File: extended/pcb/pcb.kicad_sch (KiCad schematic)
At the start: 23 parts, among them J1 LED Out +24V, J2 LED Out data, J3 LED Out GND, J4 5V out, J5 Power in 24V, J6 MEZD71201A-G, J7 Power in GND, K1 AZ943-1CH-5DE, U1 WLED, U2 74HCT245

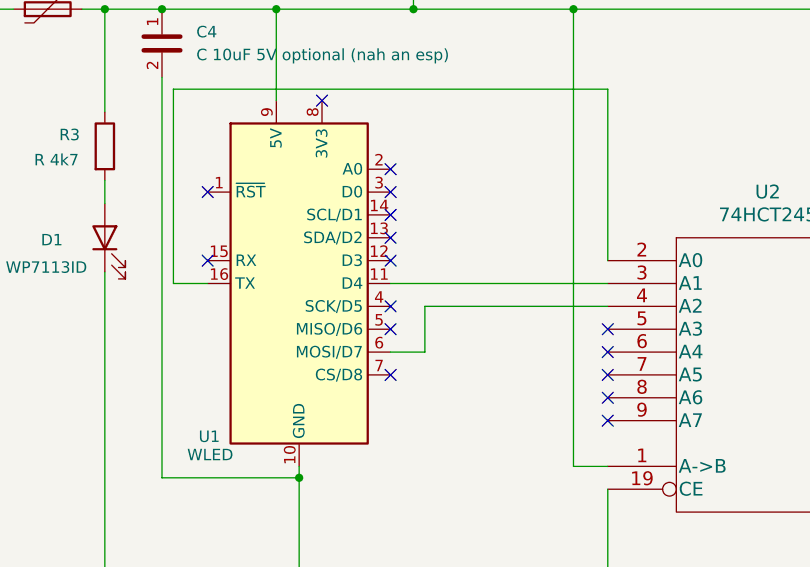
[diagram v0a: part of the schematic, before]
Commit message: fix relay flickering on boot
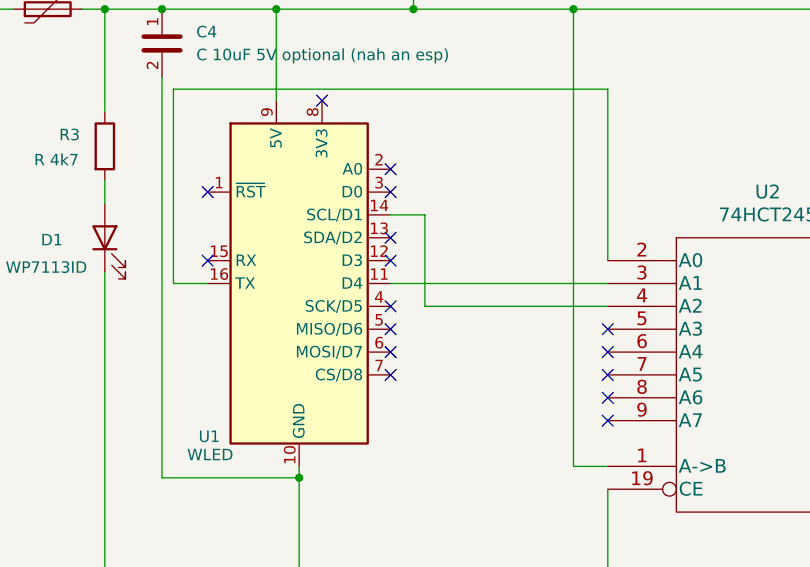
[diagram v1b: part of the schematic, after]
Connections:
- net at U2.4 (A2): now also U1.14 (SCL/D1); no longer U1.6 (MOSI/D7)
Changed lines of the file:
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@@
+	)
+	(no_connect
+		(at 116.84 93.98)
 	)
 	(no_connect
@@
 	)
 	(no_connect
-		(at 116.84 78.74)
-	)
-	(no_connect
 		(at 116.84 73.66)
 	)
@@
 	(wire
 		(pts
-			(xy 120.65 93.98) (xy 116.84 93.98)
-		)
-		(stroke
-			(width 0)
-			(type default)
-		)
-	)
-	(wire
-		(pts
 			(xy 85.09 55.88) (xy 85.09 67.31)
 		)
@@
 	(wire
 		(pts
+			(xy 116.84 78.74) (xy 120.65 78.74)
+		)
+		(stroke
+			(width 0)
+			(type default)
+		)
+	)
+	(wire
+		(pts
 			(xy 140.97 106.68) (xy 137.16 106.68)
 		)
@@
 	(wire
 		(pts
-			(xy 120.65 93.98) (xy 120.65 88.9)
-		)
-		(stroke
-			(width 0)
-			(type default)
-		)
-	)
-	(wire
-		(pts
 			(xy 106.68 106.68) (xy 106.68 107.95)
 		)
 		(stroke
+			(width 0)
+			(type default)
+		)
+	)
+	(wire
+		(pts
+			(xy 120.65 88.9) (xy 120.65 78.74)
+		)
+		(stroke

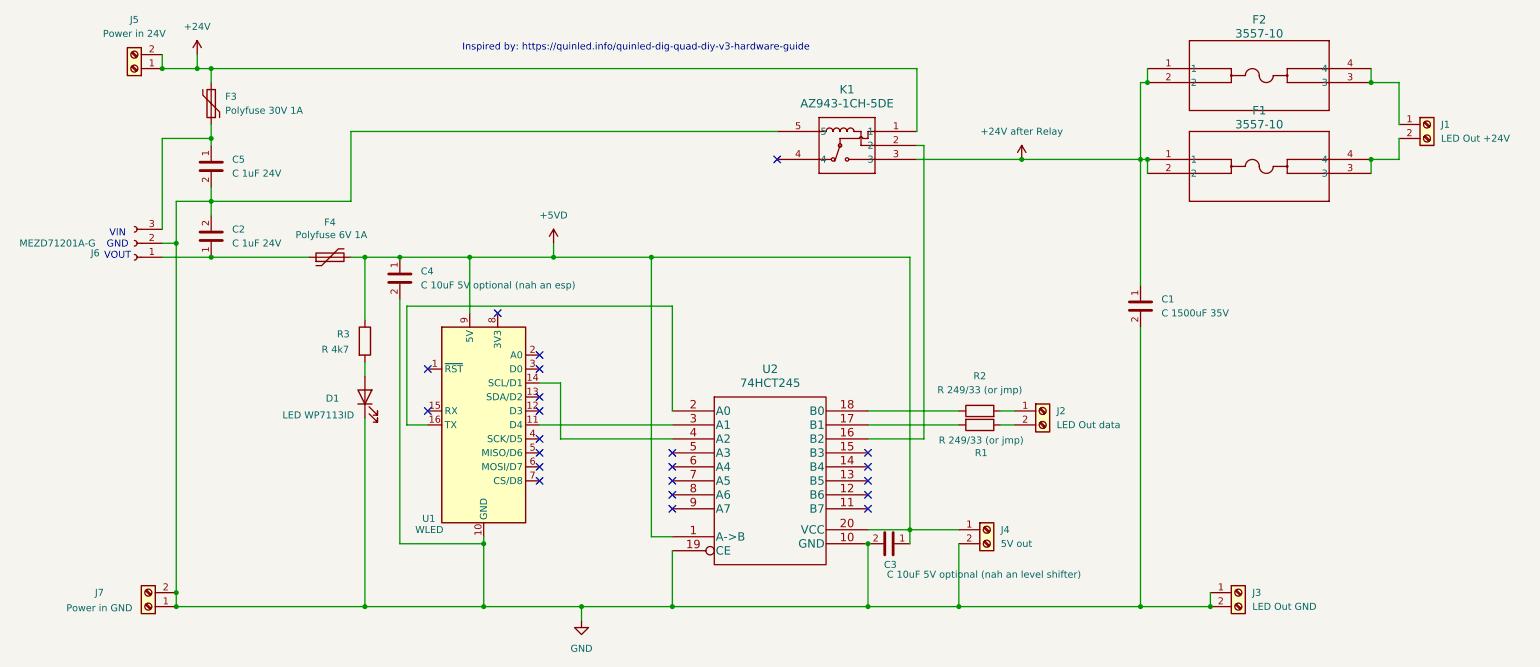
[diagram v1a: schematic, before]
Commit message: This commit is most probably wrong, but lets store it
The issue is that when the PCB is provided power then the led strip
quickly lights up, then goes of. Afterwards wled turns it on again.

I though this is because the wiring of the relay is wrong. The
documentation shows the default state to be in reverse of what the
downloadbale schematic provides
(https://www.azettler.com/pdfs/az943.pdf).
Then the relay would be on when no power is applied through the coil.

However that does not really match the sounds it makes. During the quick
on time of the led strip there are two click sounds instead of one which
should be the case if the above holds true.
Unless the relay per default clicks once when power is provided even
when the coil is low.
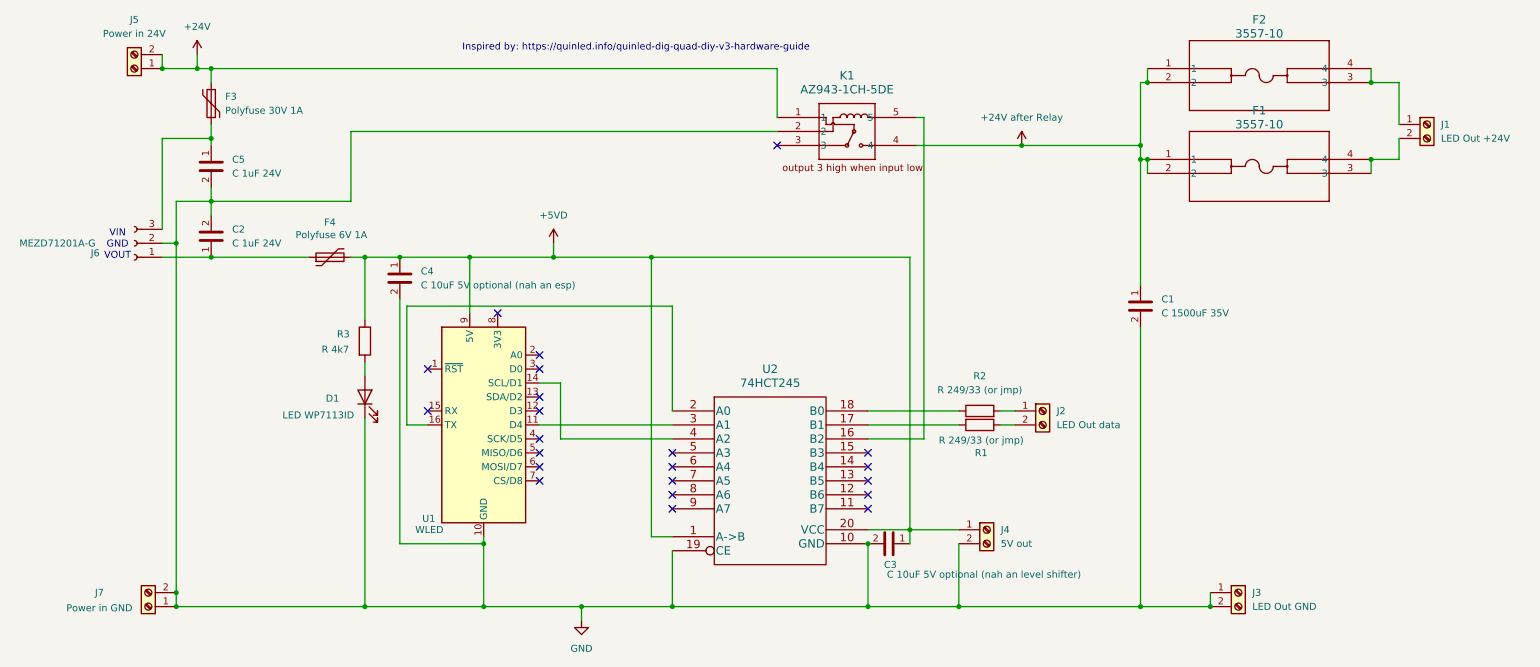
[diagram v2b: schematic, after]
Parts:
- K1: footprint Library:K_AZ943-1C_AMZ -> K_AZ943-1C_AMZ
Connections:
- net +24V after Relay: now also K1.4; no longer K1.3
- net GND: now also K1.2; no longer K1.5
- net at U2.16 (B2): now also K1.5; no longer K1.2
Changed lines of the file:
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@@
 	)
 	(junction
-		(at 204.47 38.1)
+		(at 57.15 21.59)
 		(diameter 0)
 		(color 0 0 0 0)
@@
 	)
 	(junction
+		(at 226.06 35.56)
+		(diameter 0)
+		(color 0 0 0 0)
+	)
+	(junction
 		(at 238.76 119.38)
 		(diameter 0)
@@
 	)
 	(junction
-		(at 57.15 21.59)
-		(diameter 0)
-		(color 0 0 0 0)
-	)
-	(junction
 		(at 119.38 55.88)
 		(diameter 0)
@@
 	(junction
 		(at 227.33 38.1)
+		(diameter 0)
+		(color 0 0 0 0)
+	)
+	(junction
+		(at 204.47 35.56)
 		(diameter 0)
 		(color 0 0 0 0)
@@
 	)
 	(no_connect
+		(at 160.02 35.56)
+	)
+	(no_connect
 		(at 140.97 91.44)
 	)
@@
 	)
 	(no_connect
-		(at 160.02 38.1)
-	)
-	(no_connect
 		(at 116.84 96.52)
 	)
@@
 	(wire
 		(pts
+			(xy 204.47 35.56) (xy 226.06 35.56)
+		)
+		(stroke
+			(width 0)
+			(type default)
+		)
+	)
+	(wire
+		(pts
 			(xy 57.15 55.88) (xy 74.93 55.88)
 		)
@@
 	(wire
 		(pts
-			(xy 185.42 38.1) (xy 204.47 38.1)
-		)
-		(stroke
-			(width 0)
-			(type default)
-		)
-	)
-	(wire
-		(pts
 			(xy 48.26 50.8) (xy 48.26 34.29)
 		)
@@
 	(wire
 		(pts
+			(xy 185.42 35.56) (xy 204.47 35.56)
+		)
+		(stroke
+			(width 0)
+			(type default)
+		)
+	)
+	(wire
+		(pts
 			(xy 267.97 21.59) (xy 267.97 24.13)
 		)
@@
 	(wire
 		(pts
-			(xy 185.42 21.59) (xy 185.42 33.02)
+			(xy 186.69 88.9) (xy 186.69 30.48)
 		)
 		(stroke
@@
 	(wire
 		(pts
+			(xy 226.06 35.56) (xy 226.06 38.1)
+		)
+		(stroke
+			(width 0)
+			(type default)
+		)
+	)
+	(wire
+		(pts
 			(xy 104.14 55.88) (xy 119.38 55.88)
 		)
@@
 	(wire
 		(pts
-			(xy 226.06 24.13) (xy 226.06 38.1)
+			(xy 226.06 24.13) (xy 226.06 35.56)
 		)
 		(stroke
@@
 	(wire
 		(pts
+			(xy 160.02 21.59) (xy 160.02 30.48)
+		)
+		(stroke
+			(width 0)
+			(type default)
+		)
+	)
+	(wire
+		(pts
 			(xy 227.33 38.1) (xy 227.33 40.64)
 		)
@@
 	(wire
 		(pts
-			(xy 186.69 35.56) (xy 186.69 88.9)
-		)
-		(stroke
-			(width 0)
-			(type default)
-		)
-	)
-	(wire
-		(pts
 			(xy 91.44 107.95) (xy 106.68 107.95)
 		)
@@
 	(wire
 		(pts
-			(xy 204.47 38.1) (xy 226.06 38.1)
-		)
-		(stroke
-			(width 0)
-			(type default)
-		)
-	)
-	(wire
-		(pts
 			(xy 176.53 119.38) (xy 193.04 119.38)
 		)
@@
 	(wire
 		(pts
+			(xy 186.69 30.48) (xy 185.42 30.48)
+		)
+		(stroke
+			(width 0)
+			(type default)
+		)
+	)
+	(wire
+		(pts
 			(xy 85.09 74.93) (xy 85.09 77.47)
 		)
@@
 	(wire
 		(pts
-			(xy 57.15 21.59) (xy 185.42 21.59)
-		)
-		(stroke
-			(width 0)
-			(type default)
-		)
-	)
-	(wire
-		(pts
 			(xy 267.97 38.1) (xy 273.05 38.1)
 		)
@@
 	(wire
 		(pts
-			(xy 186.69 35.56) (xy 185.42 35.56)
-		)
-		(stroke
-			(width 0)
-			(type default)
-		)
-	)
-	(wire
-		(pts
 			(xy 200.66 86.36) (xy 203.2 86.36)
 		)
@@
 		(pts
 			(xy 184.15 105.41) (xy 184.15 107.95)
+		)
+		(stroke
+			(width 0)
+			(type default)
+		)
+	)
+	(wire
+		(pts
+			(xy 57.15 21.59) (xy 160.02 21.59)
 		)
 		(stroke
@@
 	(symbol
 		(lib_id "power:+24V")
-		(at 204.47 38.1 0)
+		(at 204.47 35.56 0)
 		(unit 1)
 		(exclude_from_sim no)
@@
 		(fields_autoplaced yes)
 		(property "Reference" "#PWR04"
-			(at 204.47 41.91 0)
+			(at 204.47 39.37 0)
 			(effects
 				(font
@@
 		)
 		(property "Value" "+24V after Relay"
-			(at 204.47 33.02 0)
+			(at 204.47 30.48 0)
 			(effects
 				(font
@@
 		)
 		(property "Footprint" ""
-			(at 204.47 38.1 0)
+			(at 204.47 35.56 0)
 			(effects
 				(font
@@
 		)
 		(property "Datasheet" ""
-			(at 204.47 38.1 0)
+			(at 204.47 35.56 0)
 			(effects
 				(font
@@
 		)
 		(property "Description" "Power symbol creates a global label with name \"+24V\""
-			(at 204.47 38.1 0)
+			(at 204.47 35.56 0)
 			(effects
 				(font
@@
 	(symbol
 		(lib_id "lib:AZ943-1CH-5DE")
-		(at 185.42 33.02 0)
-		(mirror y)
+		(at 160.02 30.48 0)
 		(unit 1)
 		(exclude_from_sim no)
@@
 		(on_board yes)
 		(dnp no)
-		(fields_autoplaced yes)
 		(property "Reference" "K1"
+			(at 172.72 22.86 0)
+			(effects
+				(font
+					(size 1.524 1.524)
+				)
+			)
+		)
+		(property "Value" "AZ943-1CH-5DE"
 			(at 172.72 25.4 0)
 			(effects
@@
 			)
 		)
-		(property "Value" "AZ943-1CH-5DE"
-			(at 172.72 27.94 0)
-			(effects
-				(font
-					(size 1.524 1.524)
-				)
-			)
-		)
-		(property "Footprint" "Library:K_AZ943-1C_AMZ"
-			(at 185.42 33.02 0)
+		(property "Footprint" "K_AZ943-1C_AMZ"
+			(at 160.02 30.48 0)
 			(effects
 				(font
@@
 		)
 		(property "Datasheet" "AZ943-1CH-5DE"
-			(at 185.42 33.02 0)
+			(at 160.02 30.48 0)
 			(effects
 				(font
@@
 		)
 		(property "Description" ""
-			(at 185.42 33.02 0)
-			(effects
-				(font
+			(at 160.02 30.48 0)
+			(effects
+				(font
